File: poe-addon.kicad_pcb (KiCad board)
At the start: 2 copper layers, 61 x 20.3 mm, 36 parts, among them U1 25AA02E48T-I_OT, U2 NCP1090, U3 PG02S4803A, U4 W5500, X1 0813-1X1T-57-F, X2 Conn_01x05_Male, X3 Conn_01x05_Male, Y1 25MHz

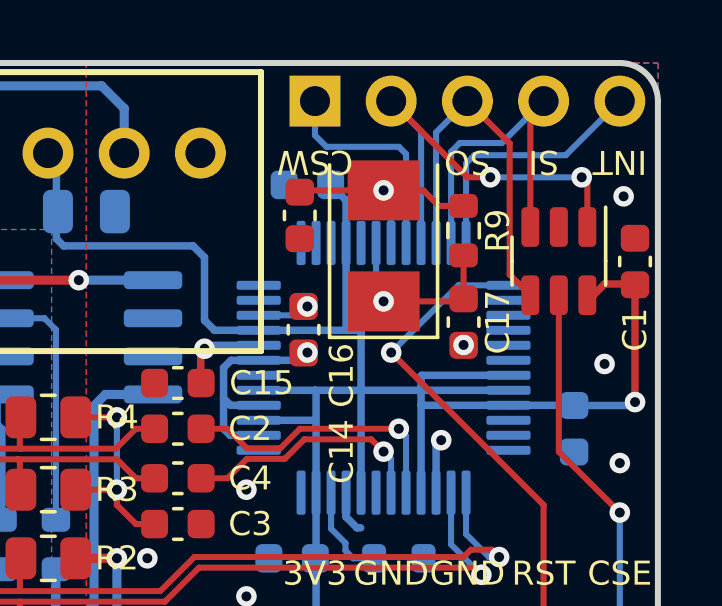
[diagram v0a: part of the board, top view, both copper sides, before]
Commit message: add pg02s 3D model
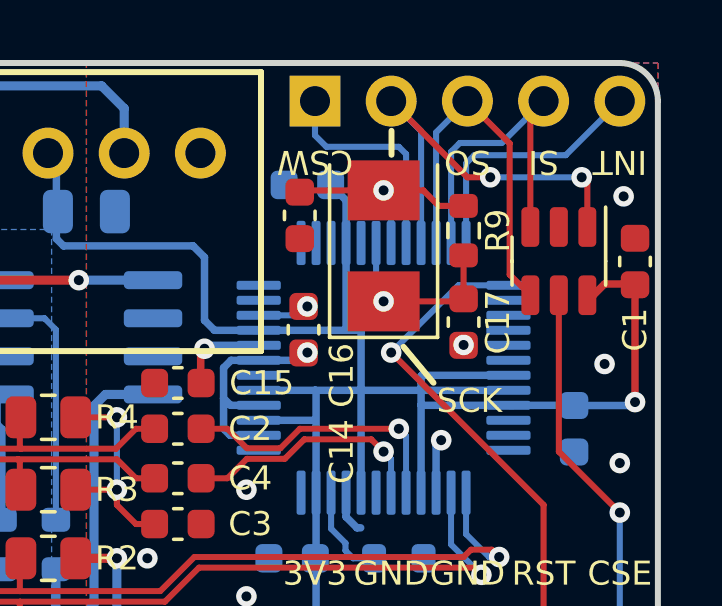
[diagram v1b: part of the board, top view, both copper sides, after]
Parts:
- U3: footprint AlexComponents:PG02S -> newam:PG02S
- X2, X3: footprint Connector_PinSocket_2.54mm:PinSocket_1x05_P2.54mm_Vertical -> Connector_PinHeader_2.54mm:PinHeader_1x05_P2.54mm_Vertical

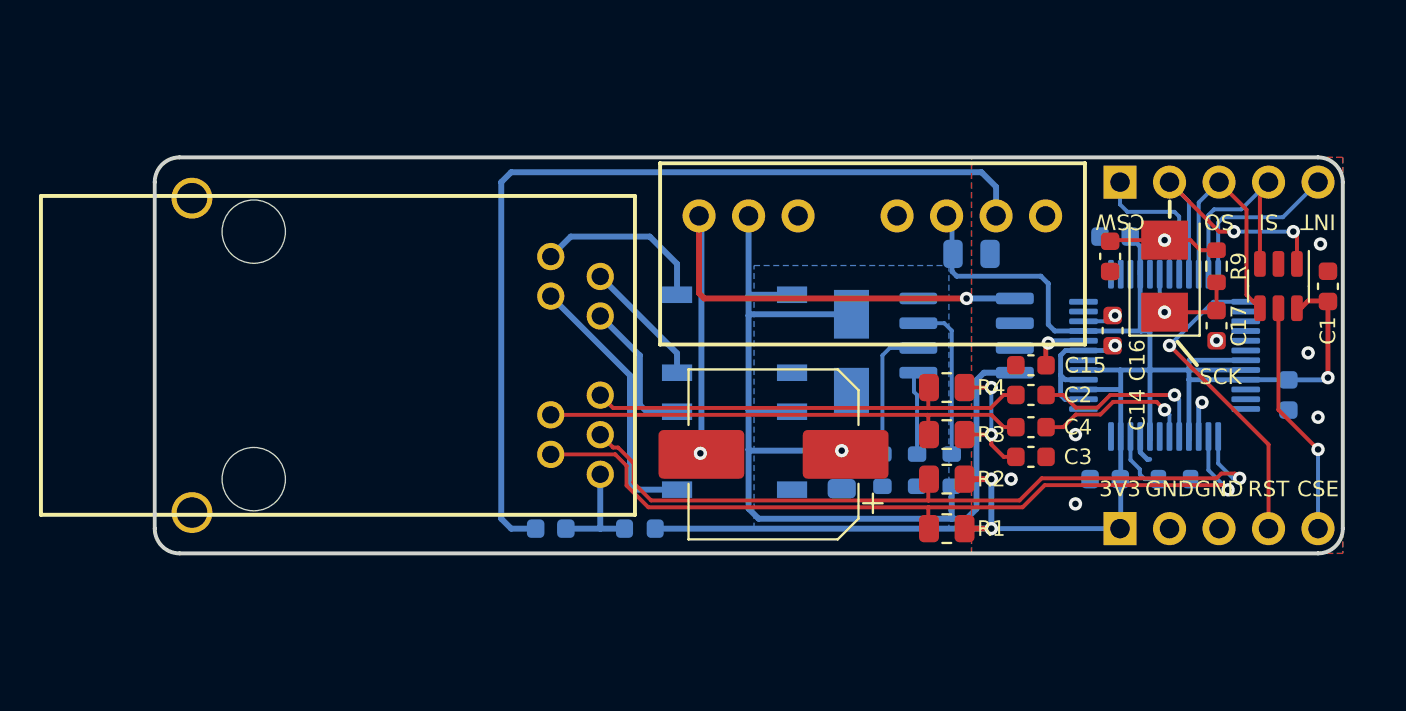
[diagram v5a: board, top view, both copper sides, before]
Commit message: add mounting holes, replace magjack with in-stock part
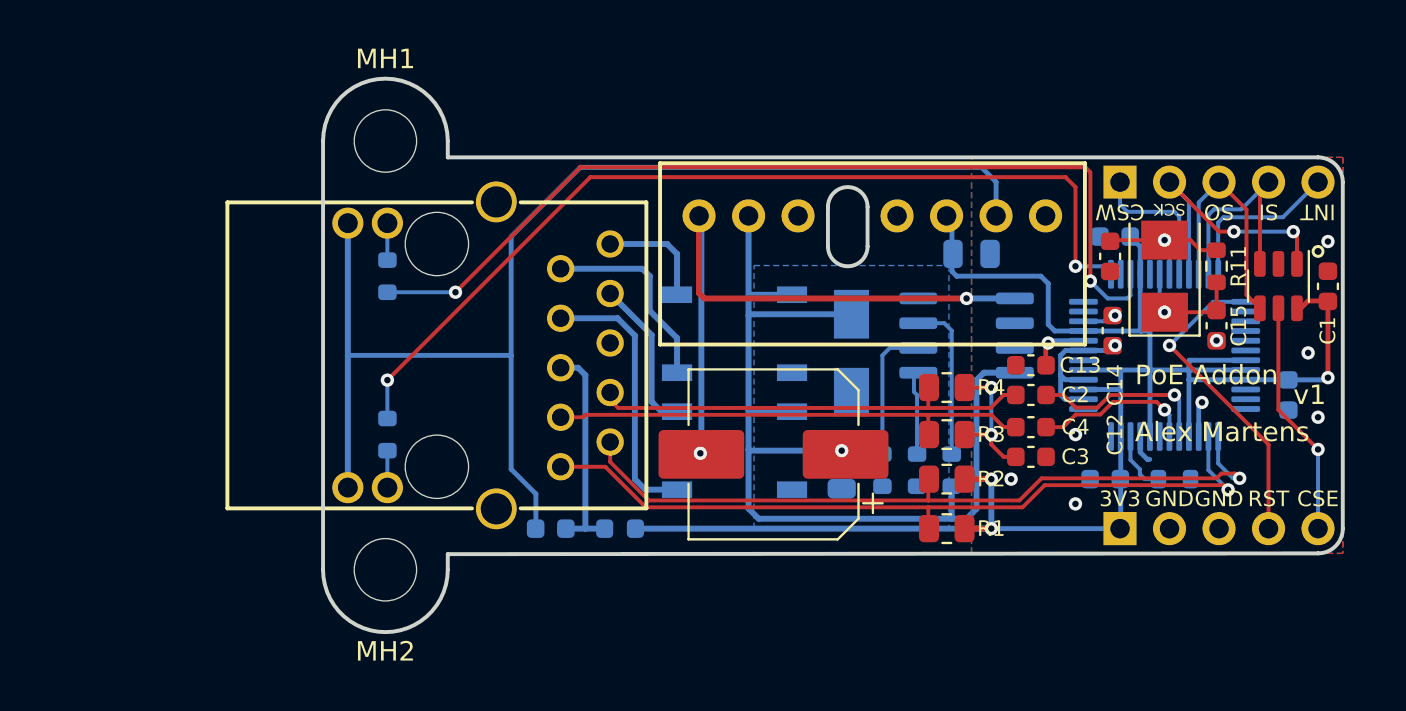
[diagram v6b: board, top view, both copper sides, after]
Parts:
- added MH1: MountingHole, MountingHole:MountingHole_3.2mm_M3, F.Cu at (57.6, 103.3)
- added MH2: MountingHole, MountingHole:MountingHole_3.2mm_M3, F.Cu at (57.6, 125.3)
- added R10: 2.2k, Resistor_SMD:R_0603_1608Metric, B.Cu at (57.7, 118.4)
- added R9: 2.2k, Resistor_SMD:R_0603_1608Metric, B.Cu at (57.7, 110.2)
- C7: value 22u -> 27u
- X1: value 0813-1X1T-57-F -> ARJM11-104; footprint newam:0813-1X1T-57-F_RJ45-Jack -> newam:ARJM11D7-104-AB-EW2
- moved X1 9.40 mm to (60.2, 114.3), turned to -90 degrees
- moved L1 1.02 mm to (69.6, 123.2)
- renumbered C12 to C10, C13 to C11, C14 to C12, C15 to C13, C16 to C14, C17 to C15, R9 to R11, X3 to X2, X2 to X3
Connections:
- D1 pad 3: /PoE PD Interface/VC12 -> /PoE PD Interface/VC45
- D1 pad 4: /PoE PD Interface/VC36 -> /PoE PD Interface/VC78
- D2 pad 3: /PoE PD Interface/VC78 -> /PoE PD Interface/VC12
- D2 pad 4: /PoE PD Interface/VC45 -> /PoE PD Interface/VC36
- U4 pad 25: unconnected-(U4-Pad25) -> Net-(R10-Pad1)
- U4 pad 27: unconnected-(U4-Pad27) -> Net-(R9-Pad1)
- X1 pad 11: /PoE PD Interface/VC78 -> LINK
- X1 pad 2: /CRXIP -> /W5500 Ethernet Interface/TXON
- X1 pad 5: /PoE PD Interface/VC12 -> /CT
- X1 pad 6: /PoE PD Interface/VC45 -> (no net)
- X1 pad 7: /CT -> /PoE PD Interface/VC45
- X1 pad 8: /W5500 Ethernet Interface/TXON -> /PoE PD Interface/VC78
- X1 pad 9: /CRXIN -> /PoE PD Interface/VC12
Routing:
- net Net-(R10-Pad1): track 0.00 -> 48.2 mm, vias 0 -> 2
- net Net-(R9-Pad1): track 0.00 -> 48.0 mm, vias 0 -> 2
- net GND: track 57.5 -> 76.7 mm
- net /CT: track 5.86 -> 11.3 mm
- net /PoE PD Interface/VC45: track 9.07 -> 13.9 mm
- net /PoE PD Interface/VC12: track 13.9 -> 10.3 mm
- net LINK: track 0.00 -> 1.90 mm
- net ACT: track 0.00 -> 1.90 mm
- net /PoE PD Interface/VC36: track 7.46 -> 5.74 mm
- net /PoE PD Interface/VC78: track 6.57 -> 7.95 mm
- net /W5500 Ethernet Interface/TXOP: track 41.1 -> 39.7 mm
- net +3V3: track 94.6 -> 95.6 mm
- net /W5500 Ethernet Interface/TXON: track 39.2 -> 38.5 mm
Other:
- board size 61 x 20.3 mm -> 52.3 x 28.4 mm
- board text added: "Alex Martens"
- board text added: "PoE Addon"
- board text added: "PoE Addon v1 Alex Martens"
- board text added: "v1"
- board text removed: "PoE Addon Alex Martens v1"
